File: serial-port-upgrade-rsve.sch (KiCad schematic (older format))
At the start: 11 parts, among them J1 MFP RC, J2 MFP TDO, J3 VCC, J4 GND, J5 Led, U1 GAL16V8_PHY, U2 12-STAGE_BINARY_RIPPLE_COUNTE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, X1 1,8432 MHz

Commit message: associate footprints, start PCB
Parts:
- C1, C2: footprint (none) -> commons-passives_THT:Passive_THT_capacitor_mlcc_W2.54mm_L7.62mm
- J1, J2, J3, J4: footprint (none) -> Connector_PinHeader_2.54mm:PinHeader_1x01_P2.54mm_Vertical
- J5: footprint (none) -> Connector_PinHeader_2.54mm:PinHeader_1x02_P2.54mm_Vertical
- R1: footprint (none) -> commons-passives_THT:Passive_THT_resistor_W2.54mm_L10.16mm
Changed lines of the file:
@@
 F 0 "J2" H 1500 2100 50  0000 C CNN
 F 1 "MFP TDO" H 1500 1900 50  0000 C CNN
-F 2 "" H 1500 2000 50  0001 C CNN
+F 2 "Connector_PinHeader_2.54mm:PinHeader_1x01_P2.54mm_Vertical" H 1500 2000 50  0001 C CNN
 F 3 "~" H 1500 2000 50  0001 C CNN
 	1    1500 2000
@@
 F 0 "J1" H 1500 1600 50  0000 C CNN
 F 1 "MFP RC" H 1500 1400 50  0000 C CNN
-F 2 "" H 1500 1500 50  0001 C CNN
+F 2 "Connector_PinHeader_2.54mm:PinHeader_1x01_P2.54mm_Vertical" H 1500 1500 50  0001 C CNN
 F 3 "~" H 1500 1500 50  0001 C CNN
 	1    1500 1500
@@
 F 0 "J5" H 3500 1600 50  0000 C CNN
 F 1 "Led" H 3500 1300 50  0000 C CNN
-F 2 "" H 3500 1500 50  0001 C CNN
+F 2 "Connector_PinHeader_2.54mm:PinHeader_1x02_P2.54mm_Vertical" H 3500 1500 50  0001 C CNN
 F 3 "~" H 3500 1500 50  0001 C CNN
 	1    3500 1500
@@
 F 0 "R1" H 6300 5750 50  0000 L CNN
 F 1 "1K" H 6300 5650 50  0000 L CNN
-F 2 "" H 6250 5700 50  0001 C CNN
+F 2 "commons-passives_THT:Passive_THT_resistor_W2.54mm_L10.16mm" H 6250 5700 50  0001 C CNN
 F 3 "~" H 6250 5700 50  0001 C CNN
 	1    6250 5700
@@
 F 0 "C1" H 6850 5750 50  0000 L CNN
 F 1 "0.1uF" H 6850 5650 50  0000 L CNN
-F 2 "" H 6750 5700 50  0001 C CNN
+F 2 "commons-passives_THT:Passive_THT_capacitor_mlcc_W2.54mm_L7.62mm" H 6750 5700 50  0001 C CNN
 F 3 "~" H 6750 5700 50  0001 C CNN
 	1    6750 5700
@@
 F 0 "J3" H 1500 2600 50  0000 C CNN
 F 1 "VCC" H 1500 2400 50  0000 C CNN
-F 2 "" H 1500 2500 50  0001 C CNN
+F 2 "Connector_PinHeader_2.54mm:PinHeader_1x01_P2.54mm_Vertical" H 1500 2500 50  0001 C CNN
 F 3 "~" H 1500 2500 50  0001 C CNN
 	1    1500 2500
@@
 F 0 "J4" H 1500 3100 50  0000 C CNN
 F 1 "GND" H 1500 2900 50  0000 C CNN
-F 2 "" H 1500 3000 50  0001 C CNN
+F 2 "Connector_PinHeader_2.54mm:PinHeader_1x01_P2.54mm_Vertical" H 1500 3000 50  0001 C CNN
 F 3 "~" H 1500 3000 50  0001 C CNN
 	1    1500 3000
@@
 F 0 "C2" H 1450 5950 50  0000 L CNN
 F 1 "0.1uF" H 1450 5850 50  0000 L CNN
-F 2 "" H 1350 5900 50  0001 C CNN
+F 2 "commons-passives_THT:Passive_THT_capacitor_mlcc_W2.54mm_L7.62mm" H 1350 5900 50  0001 C CNN
 F 3 "~" H 1350 5900 50  0001 C CNN
 	1    1350 5900

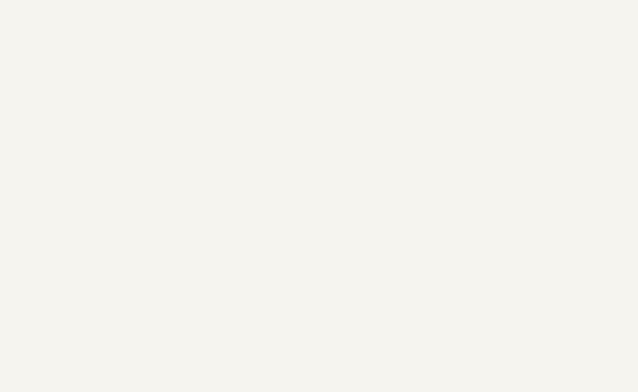
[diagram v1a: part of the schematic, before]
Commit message: added IDC connector, adjusted reference label position
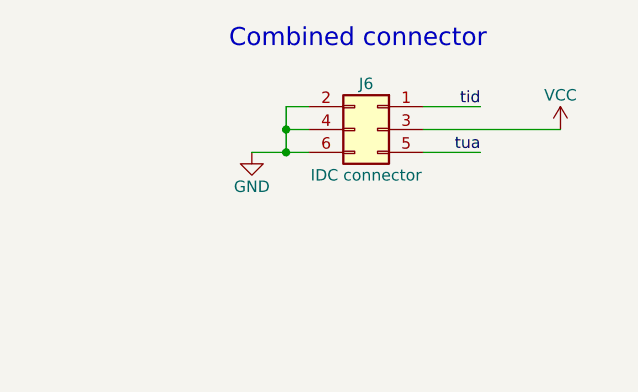
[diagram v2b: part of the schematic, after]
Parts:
- added J6: IDC connector, Connector_IDC:IDC-Header_2x03_P2.54mm_Horizontal, symbol Connector_Generic:Conn_02x03_Odd_Even
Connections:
- net GND: now also J6.2 (Pin_2), J6.4 (Pin_4), J6.6 (Pin_6)
- net VCC: now also J6.3 (Pin_3)
- net tid: now also J6.1 (Pin_1)
- net tua: now also J6.5 (Pin_5)
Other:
- note added: "Combined connector"
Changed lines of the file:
@@
 Wire Wire Line
 	1350 6100 1350 6000
+$Comp
+L Connector_Generic:Conn_02x03_Odd_Even J6
+U 1 1 636DF6D3
+P 6050 1600
+F 0 "J6" H 6100 1800 50  0000 C CNN
+F 1 "IDC connector" H 6100 1400 50  0000 C CNN
+F 2 "Connector_IDC:IDC-Header_2x03_P2.54mm_Horizontal" H 6050 1600 50  0001 C CNN
+F 3 "~" H 6050 1600 50  0001 C CNN
+	1    6050 1600
+	-1   0    0    -1
+$EndComp
+Text Notes 5400 1250 0    79   ~ 0
+Combined connector
+$Comp
+L power:GND #PWR012
+U 1 1 636DFE0C
+P 5500 1700
+F 0 "#PWR012" H 5500 1450 50  0001 C CNN
+F 1 "GND" H 5500 1550 50  0000 C CNN
+F 2 "" H 5500 1700 50  0001 C CNN
+F 3 "" H 5500 1700 50  0001 C CNN
+	1    5500 1700
+	1    0    0    -1
+$EndComp
+$Comp
+L power:VCC #PWR011
+U 1 1 636E0666
+P 6850 1600
+F 0 "#PWR011" H 6850 1450 50  0001 C CNN
+F 1 "VCC" H 6850 1750 50  0000 C CNN
+F 2 "" H 6850 1600 50  0001 C CNN
+F 3 "" H 6850 1600 50  0001 C CNN
+	1    6850 1600
+	1    0    0    -1
+$EndComp
+Wire Wire Line
+	5650 1500 5650 1600
+Wire Wire Line
+	5650 1700 5500 1700
+Wire Wire Line
+	5650 1500 5750 1500
+Wire Wire Line
+	5650 1600 5750 1600
+Connection ~ 5650 1600
+Wire Wire Line
+	5650 1600 5650 1700
+Wire Wire Line
+	5650 1700 5750 1700
+Connection ~ 5650 1700
+Wire Wire Line
+	6250 1500 6500 1500
+Wire Wire Line
+	6250 1700 6500 1700
+Wire Wire Line
+	6250 1600 6850 1600
+Text Label 6500 1700 2    50   ~ 0
+tua
+Text Label 6500 1500 2    50   ~ 0
+tid
 $EndSCHEMATC

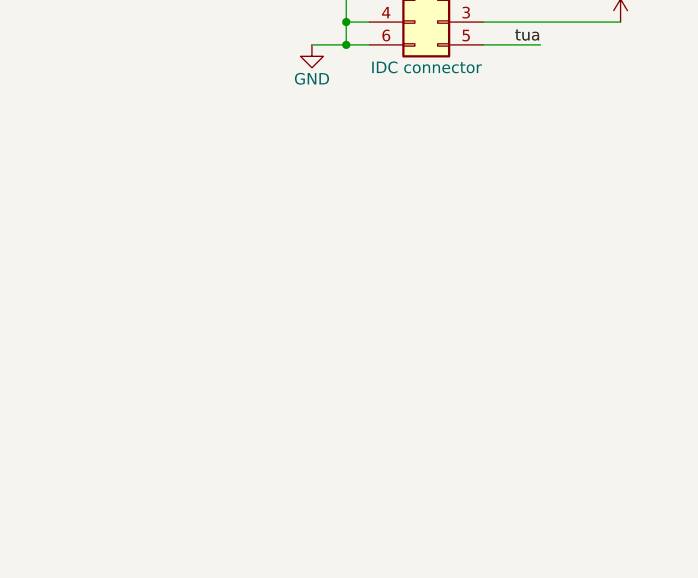
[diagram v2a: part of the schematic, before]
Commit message: added mounting hole
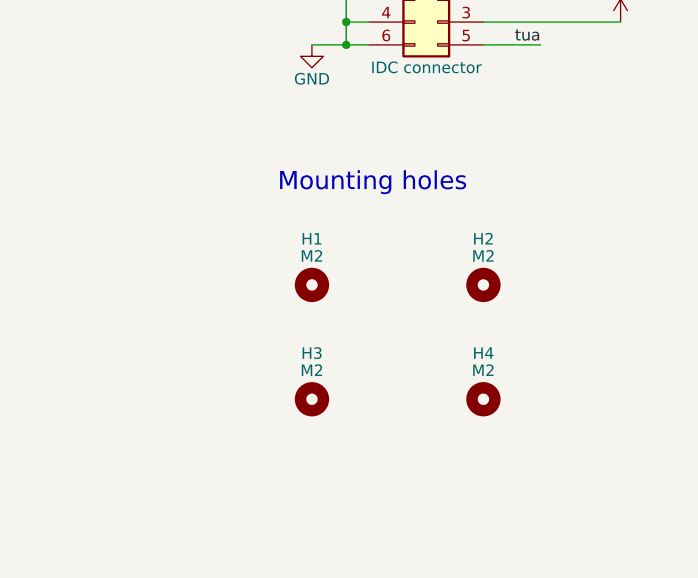
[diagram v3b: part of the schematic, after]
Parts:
- added H1, H2, H3, H4: M2, MountingHole:MountingHole_2.2mm_M2, symbol Mechanical:MountingHole
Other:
- note added: "Mounting holes"
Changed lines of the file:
@@
 Text Label 6500 1500 2    50   ~ 0
 tid
+$Comp
+L Mechanical:MountingHole H1
+U 1 1 636F960F
+P 5500 2750
+F 0 "H1" H 5500 2950 50  0000 C CNN
+F 1 "M2" H 5500 2875 50  0000 C CNN
+F 2 "MountingHole:MountingHole_2.2mm_M2" H 5500 2750 50  0001 C CNN
+F 3 "~" H 5500 2750 50  0001 C CNN
+	1    5500 2750
+	1    0    0    -1
+$EndComp
+$Comp
+L Mechanical:MountingHole H2
+U 1 1 636F9BFE
+P 6250 2750
+F 0 "H2" H 6250 2950 50  0000 C CNN
+F 1 "M2" H 6250 2875 50  0000 C CNN
+F 2 "MountingHole:MountingHole_2.2mm_M2" H 6250 2750 50  0001 C CNN
+F 3 "~" H 6250 2750 50  0001 C CNN
+	1    6250 2750
+	1    0    0    -1
+$EndComp
+$Comp
+L Mechanical:MountingHole H3
+U 1 1 636FA348
+P 5500 3250
+F 0 "H3" H 5500 3450 50  0000 C CNN
+F 1 "M2" H 5500 3375 50  0000 C CNN
+F 2 "MountingHole:MountingHole_2.2mm_M2" H 5500 3250 50  0001 C CNN
+F 3 "~" H 5500 3250 50  0001 C CNN
+	1    5500 3250
+	1    0    0    -1
+$EndComp
+$Comp
+L Mechanical:MountingHole H4
+U 1 1 636FA646
+P 6250 3250
+F 0 "H4" H 6250 3450 50  0000 C CNN
+F 1 "M2" H 6250 3375 50  0000 C CNN
+F 2 "MountingHole:MountingHole_2.2mm_M2" H 6250 3250 50  0001 C CNN
+F 3 "~" H 6250 3250 50  0001 C CNN
+	1    6250 3250
+	1    0    0    -1
+$EndComp
+Text Notes 5350 2350 0    79   ~ 0
+Mounting holes
 $EndSCHEMATC

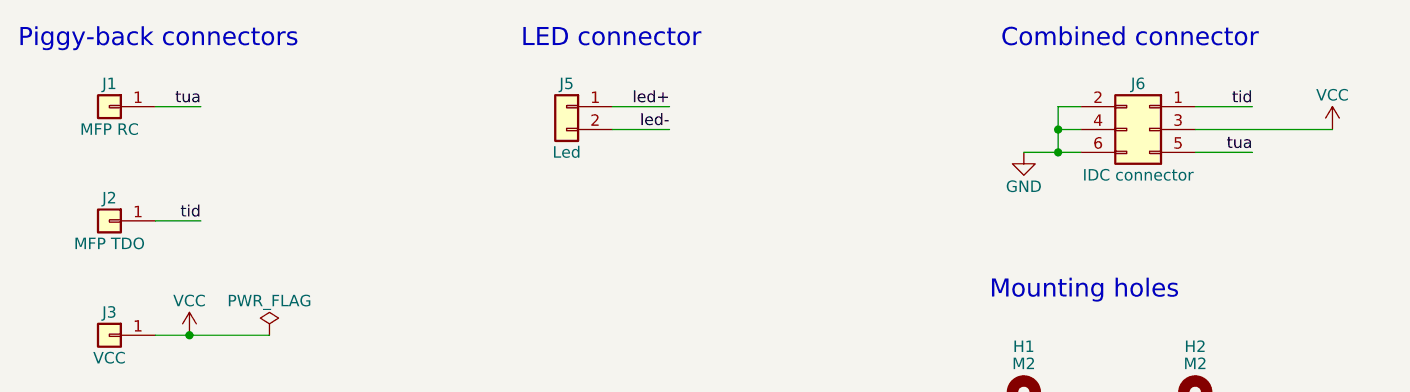
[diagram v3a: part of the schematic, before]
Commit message: schematic : change 'piggy back' to 'individuals', and reorganize layout
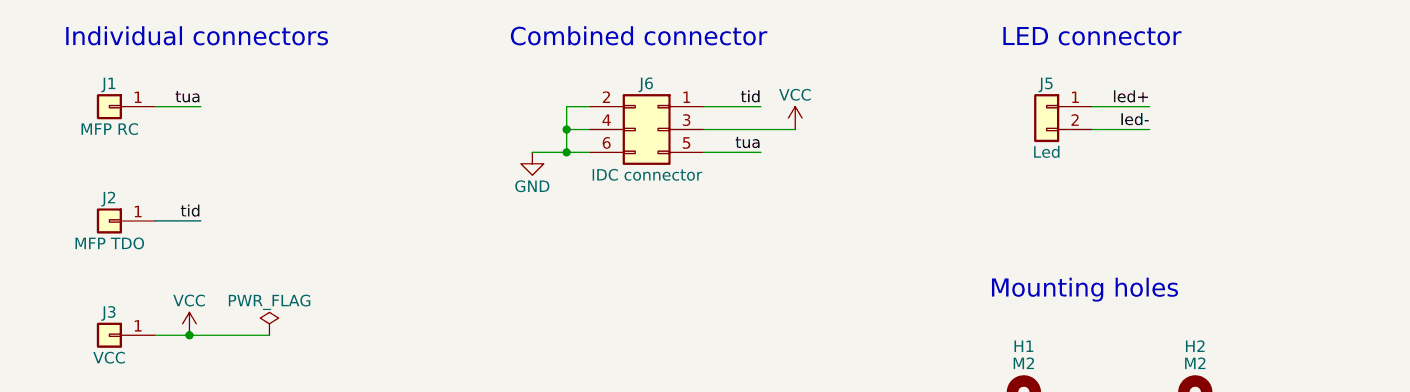
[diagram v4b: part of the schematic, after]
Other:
- note added: "Individual connectors"
- note removed: "Piggy-back connectors"
- moved on the sheet: J5, J6
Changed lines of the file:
@@
 Sheet 1 1
 Title "RSVE, higher baudrates for the serial port of the Atari ST"
-Date "2022-11-08"
-Rev "v0.0.0-draft"
+Date "2022-11-10"
+Rev "v1.0.0"
 Comp "Remake by Sporniket"
 Comment1 ""
@@
 L Connector_Generic:Conn_01x02 J5
 U 1 1 636C3721
-P 3500 1500
-F 0 "J5" H 3500 1600 50  0000 C CNN
-F 1 "Led" H 3500 1300 50  0000 C CNN
-F 2 "Connector_PinHeader_2.54mm:PinHeader_1x02_P2.54mm_Vertical" H 3500 1500 50  0001 C CNN
-F 3 "~" H 3500 1500 50  0001 C CNN
-	1    3500 1500
-	-1   0    0    -1
-$EndComp
-Text Label 3950 1500 2    50   ~ 0
+P 5600 1500
+F 0 "J5" H 5600 1600 50  0000 C CNN
+F 1 "Led" H 5600 1300 50  0000 C CNN
+F 2 "Connector_PinHeader_2.54mm:PinHeader_1x02_P2.54mm_Vertical" H 5600 1500 50  0001 C CNN
+F 3 "~" H 5600 1500 50  0001 C CNN
+	1    5600 1500
+	-1   0    0    -1
+$EndComp
+Text Label 6050 1500 2    50   ~ 0
 led+
-Text Label 3950 1600 2    50   ~ 0
+Text Label 6050 1600 2    50   ~ 0
 led-
 Wire Wire Line
-	3950 1600 3700 1600
-Wire Wire Line
-	3700 1500 3950 1500
-Text Notes 1100 1250 0    79   ~ 0
-Piggy-back connectors
-Text Notes 3300 1250 0    79   ~ 0
+	6050 1600 5800 1600
+Wire Wire Line
+	5800 1500 6050 1500
+Text Notes 1300 1250 0    79   ~ 0
+Individual connectors
+Text Notes 5400 1250 0    79   ~ 0
 LED connector
 $Comp
@@
 L Connector_Generic:Conn_02x03_Odd_Even J6
 U 1 1 636DF6D3
-P 6050 1600
-F 0 "J6" H 6100 1800 50  0000 C CNN
-F 1 "IDC connector" H 6100 1400 50  0000 C CNN
-F 2 "Connector_IDC:IDC-Header_2x03_P2.54mm_Horizontal" H 6050 1600 50  0001 C CNN
-F 3 "~" H 6050 1600 50  0001 C CNN
-	1    6050 1600
-	-1   0    0    -1
-$EndComp
-Text Notes 5400 1250 0    79   ~ 0
+P 3900 1600
+F 0 "J6" H 3950 1800 50  0000 C CNN
+F 1 "IDC connector" H 3950 1400 50  0000 C CNN
+F 2 "Connector_IDC:IDC-Header_2x03_P2.54mm_Horizontal" H 3900 1600 50  0001 C CNN
+F 3 "~" H 3900 1600 50  0001 C CNN
+	1    3900 1600
+	-1   0    0    -1
+$EndComp
+Text Notes 3250 1250 0    79   ~ 0
 Combined connector
 $Comp
 L power:GND #PWR012
 U 1 1 636DFE0C
-P 5500 1700
-F 0 "#PWR012" H 5500 1450 50  0001 C CNN
-F 1 "GND" H 5500 1550 50  0000 C CNN
-F 2 "" H 5500 1700 50  0001 C CNN
-F 3 "" H 5500 1700 50  0001 C CNN
-	1    5500 1700
+P 3350 1700
+F 0 "#PWR012" H 3350 1450 50  0001 C CNN
+F 1 "GND" H 3350 1550 50  0000 C CNN
+F 2 "" H 3350 1700 50  0001 C CNN
+F 3 "" H 3350 1700 50  0001 C CNN
+	1    3350 1700
 	1    0    0    -1
 $EndComp
@@
 L power:VCC #PWR011
 U 1 1 636E0666
-P 6850 1600
-F 0 "#PWR011" H 6850 1450 50  0001 C CNN
-F 1 "VCC" H 6850 1750 50  0000 C CNN
-F 2 "" H 6850 1600 50  0001 C CNN
-F 3 "" H 6850 1600 50  0001 C CNN
-	1    6850 1600
-	1    0    0    -1
-$EndComp
-Wire Wire Line
-	5650 1500 5650 1600
-Wire Wire Line
-	5650 1700 5500 1700
-Wire Wire Line
-	5650 1500 5750 1500
-Wire Wire Line
-	5650 1600 5750 1600
-Connection ~ 5650 1600
-Wire Wire Line
-	5650 1600 5650 1700
-Wire Wire Line
-	5650 1700 5750 1700
-Connection ~ 5650 1700
-Wire Wire Line
-	6250 1500 6500 1500
-Wire Wire Line
-	6250 1700 6500 1700
-Wire Wire Line
-	6250 1600 6850 1600
-Text Label 6500 1700 2    50   ~ 0
+P 4500 1600
+F 0 "#PWR011" H 4500 1450 50  0001 C CNN
+F 1 "VCC" H 4500 1750 50  0000 C CNN
+F 2 "" H 4500 1600 50  0001 C CNN
+F 3 "" H 4500 1600 50  0001 C CNN
+	1    4500 1600
+	1    0    0    -1
+$EndComp
+Wire Wire Line
+	3500 1500 3500 1600
+Wire Wire Line
+	3500 1700 3350 1700
+Wire Wire Line
+	3500 1500 3600 1500
+Wire Wire Line
+	3500 1600 3600 1600
+Connection ~ 3500 1600
+Wire Wire Line
+	3500 1600 3500 1700
+Wire Wire Line
+	3500 1700 3600 1700
+Connection ~ 3500 1700
+Wire Wire Line
+	4100 1500 4350 1500
+Wire Wire Line
+	4100 1700 4350 1700
+Text Label 4350 1700 2    50   ~ 0
 tua
-Text Label 6500 1500 2    50   ~ 0
+Text Label 4350 1500 2    50   ~ 0
 tid
 $Comp
@@
 Text Notes 5350 2350 0    79   ~ 0
 Mounting holes
+Wire Wire Line
+	4100 1600 4500 1600
 $EndSCHEMATC
